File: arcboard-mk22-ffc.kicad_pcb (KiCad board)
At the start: 2 copper layers, 313 x 104.2 mm, 21 parts, among them J10 Conn_01x60, J7 Conn_01x04, J8 Conn_01x04

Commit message: fixing folding issues, fattening up the led boards
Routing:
- net +5V: track 2504.9 -> 2516.9 mm, vias 30 -> 31
- net ROW10: track 352.4 -> 362.2 mm
- net GND: track 3088.7 -> 3094.5 mm
- net KEYS_DO: track 499.8 -> 505.5 mm
- net Main_LED_OUT: track 331.6 -> 337.0 mm
- net COL0: track 915.2 -> 919.8 mm
- net ENCODER2_R1: track 313.3 -> 309.6 mm
- net ENCODER2_R2: track 313.1 -> 309.4 mm
- net COL3: track 946.5 -> 947.2 mm
- net COL4: track 893.1 -> 893.7 mm

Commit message: fixing more cray, starting silkscreen
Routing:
- net +5V: track 2516.9 -> 2506.5 mm
- net ROW4: track 655.3 -> 645.9 mm, vias 13 -> 14
- net ROW2: track 606.3 -> 599.9 mm
- net ROW3: track 598.4 -> 595.6 mm
- net COL0: track 919.8 -> 917.7 mm
- net SPI1_CLK: track 511.8 -> 510.5 mm
- net ROW6: track 640.8 -> 642.0 mm
- net ROW5: track 661.6 -> 660.7 mm
- net ROW1: track 603.4 -> 604.3 mm
- net Net-(COL-4-Pin_2): track 117.8 -> 118.6 mm
- net ROW10: track 362.2 -> 361.6 mm
- net SPI1_MOSI: track 504.4 -> 505.0 mm
- net ENCODER2_R2: track 309.4 -> 308.9 mm
- net Net-(COL-0-Pin_2): track 110.1 -> 109.6 mm
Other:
- board text added: "COL0"
- board text added: "COL1"
- board text added: "COL2"
- board text added: "COL3"
- board text added: "COL4"
- board text added: "COL5"
- board text added: "^^^ FOLD ^^^"
- board text added: "vvv FOLD vvv"

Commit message: first draft silkscreen
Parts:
- added LOGO1: **REF, kicad-libraries:awesome-logo, F.Cu at (13.0, 15.1)
- added LOGO2: **REF, kicad-libraries:awesome-logo, B.Cu at (12.9, 15.0)
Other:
- board text added: "ENCODER ONE"
- board text added: "ENCODER TWO"
- board text added: "FIVE"
- board text added: "FOLD"
- board text added: "FOUR"
- board text added: "ONE"
- board text added: "THREE"
- board text added: "THUMB FIVE"
- board text added: "THUMB FOUR"
- board text added: "THUMB ONE"
- board text added: "THUMB THREE"
- board text added: "THUMB TWO"
- board text added: "TWO"
- board text added: "arcboard-mk22-ffc"
- board text added: "zero"
- board text removed: "COL0"
- board text removed: "COL1"
- board text removed: "COL2"
- board text removed: "COL3"
- board text removed: "COL4"
- board text removed: "COL5"
- board text removed: "THUMB1"
- board text removed: "^^^ FOLD ^^^"
- board text removed: "vvv FOLD vvv"

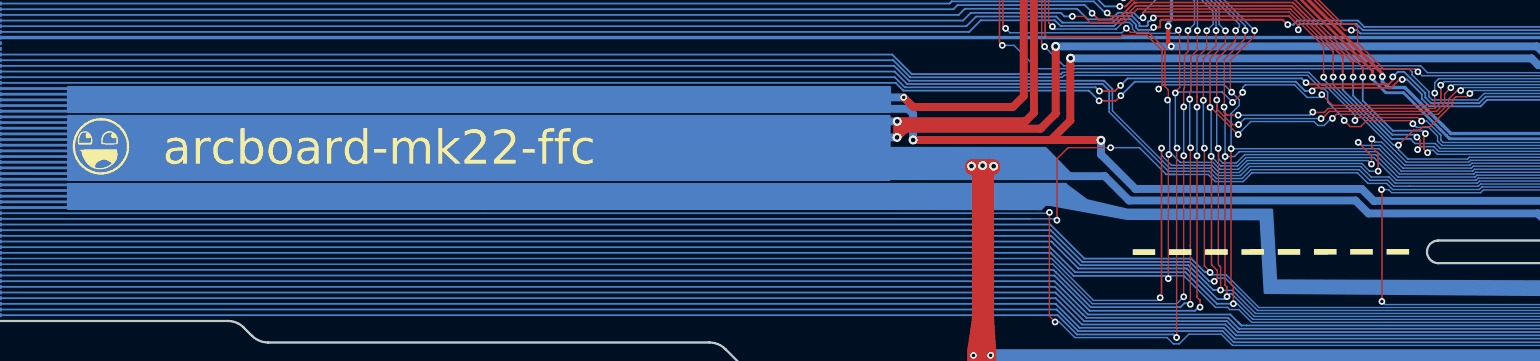
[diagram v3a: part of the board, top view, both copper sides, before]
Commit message: silkscreen changes, cleanup prior to easy-eda
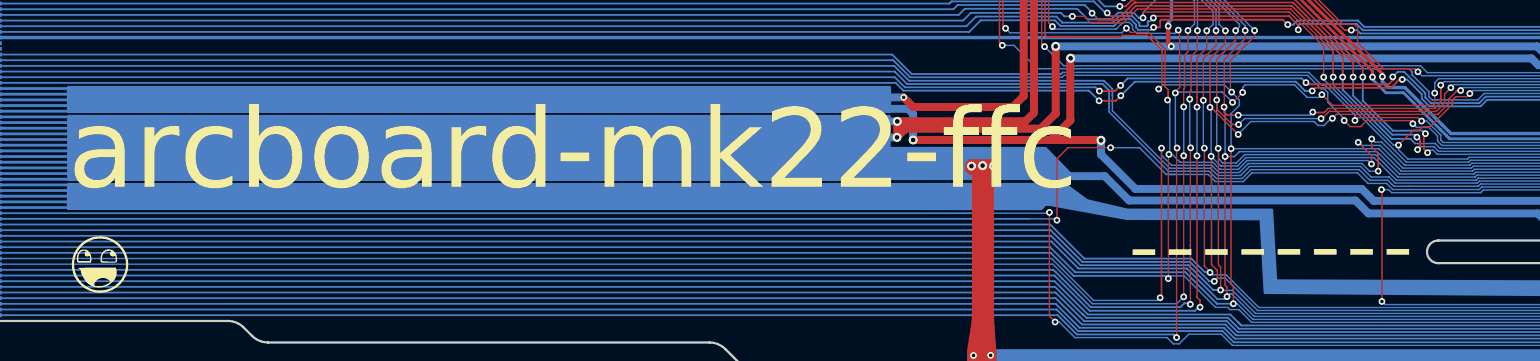
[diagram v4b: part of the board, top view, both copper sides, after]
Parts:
- moved LOGO1 10.4 mm to (12.9, 25.5)
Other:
- board text removed: "COL-0"
- board text removed: "COL-1"
- board text removed: "COL-2"
- board text removed: "COL-3"
- board text removed: "COL-4"
- board text removed: "COL-5"
- board text removed: "THUMB2"
- board text removed: "THUMB3"
- board text removed: "THUMB4"
- board text removed: "THUMB5"
- board text removed: "TOP-ENCODER1"
- board text removed: "TOP-ENCODER2"

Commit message: silkscreen changes, fixing drc issues
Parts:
- moved LOGO1 22.4 mm to (10.1, 3.35)
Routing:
- net COL0: track 917.7 -> 919.6 mm
- net ROW7: track 204.1 -> 204.6 mm
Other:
- board text added: "github.com/christrotter/arcboard-mk22-ffc"
- board text added: "pairs with: github.com/christrotter/arcboard-stm32-mk2"

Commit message: first draft readme
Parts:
- moved LOGO2 12.0 mm to (10.1, 3.38), turned to 180 degrees
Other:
- board text added: "LEFT"
- board text added: "RIGHT"
